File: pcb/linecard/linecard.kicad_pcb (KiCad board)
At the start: 6 copper layers, 716 parts, among them J1 CONN_ATX12V, J10 ARF6-08-S-D-A-K-TR, J11 SMPM, J12 SMPM, J13 XILINX_JTAG, J14 ARF6-08-S-D-A-K-TR, J2 LPJG47036AWNL, J3 CORTEX_DEBUG_ETM, J4 0532611071, J5 LPJG47036AWNL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

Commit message: Began layout of first few ports and left VSC8512
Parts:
- added R100: 1K, azonenberg_pcb:EIA_0402_RES_NOSILK, F.Cu at (65.0, 45.0)
- added R101: 10K, azonenberg_pcb:EIA_0402_RES_NOSILK, F.Cu at (65.0, 46.5)
- added TP23: TESTPOINT, azonenberg_pcb:TESTPOINT_SMT_0.5MM, F.Cu at (69.0, 45.0)
- added TP24: TESTPOINT, azonenberg_pcb:TESTPOINT_SMT_0.5MM, F.Cu at (69.0, 48.5)
- C100, C101, C102, C103, C104, C107, C108, C109, C110, C111, C112, C113, C116, C117, C118, C119, C120, C121, C124, C125, C126, C127, C128, C129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: moved to B.Cu
- R59, R92: value 10K -> 1K
- moved C146 152.5 mm to (-22.4, 91.7)
- moved C158 152.5 mm to (-19.3, 81.7)
- moved C162 152.5 mm to (-16.0, 72.7)
- moved C163 152.5 mm to (-16.0, 74.5)
- moved C169 152.5 mm to (-16.0, 76.3)
- moved C174 152.5 mm to (-16.0, 78.1)
- moved C61 152.5 mm to (-22.4, 83.9)
- moved C63 152.5 mm to (-22.4, 86.5)
- moved C76 152.5 mm to (-22.4, 89.1)
- moved C87 152.5 mm to (-19.3, 72.7)
- moved C94 152.5 mm to (-19.3, 76.3)
- moved C36 152.5 mm to (-22.6, 72.7)
- moved C39 152.5 mm to (-22.6, 74.5)
- moved C85 152.5 mm to (-22.6, 81.7)
- moved J10 152.4 mm to (36.4, 35.2)
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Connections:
- U10 pad R2: unconnected-(U10A-MDINT-PadR2) -> Net-(TP23-P1)
- U11 pad 4: /PHY 0 MDI/PHY0_M1_N -> /PHY 0 MDI/PHY0_M1_P
- U11 pad 5: /PHY 0 MDI/PHY0_M1_P -> /PHY 0 MDI/PHY0_M1_N
- U11 pad 6: /PHY 0 MDI/PHY0_D1_P -> /PHY 0 MDI/PHY0_D1_N
- U11 pad 7: /PHY 0 MDI/PHY0_D1_N -> /PHY 0 MDI/PHY0_D1_P
- U12 pad 1: /PHY 0 MDI/PHY0_M2_N -> /PHY 0 MDI/PHY0_M2_P
- U12 pad 10: /PHY 0 MDI/PHY0_D2_N -> /PHY 0 MDI/PHY0_D2_P
- U12 pad 2: /PHY 0 MDI/PHY0_M2_P -> /PHY 0 MDI/PHY0_M2_N
- U12 pad 9: /PHY 0 MDI/PHY0_D2_P -> /PHY 0 MDI/PHY0_D2_N
- U13 pad 1: /PHY 0 MDI/PHY1_M0_N -> /PHY 0 MDI/PHY1_M2_N
- U13 pad 10: /PHY 0 MDI/PHY1_D0_N -> /PHY 0 MDI/PHY1_D2_N
- U13 pad 2: /PHY 0 MDI/PHY1_M0_P -> /PHY 0 MDI/PHY1_M2_P
- U13 pad 4: /PHY 0 MDI/PHY1_M1_N -> /PHY 0 MDI/PHY1_M3_P
- U13 pad 5: /PHY 0 MDI/PHY1_M1_P -> /PHY 0 MDI/PHY1_M3_N
- U13 pad 6: /PHY 0 MDI/PHY1_D1_P -> /PHY 0 MDI/PHY1_D3_N
- U13 pad 7: /PHY 0 MDI/PHY1_D1_N -> /PHY 0 MDI/PHY1_D3_P
- U13 pad 9: /PHY 0 MDI/PHY1_D0_P -> /PHY 0 MDI/PHY1_D2_P
- U14 pad 1: /PHY 0 MDI/PHY1_M2_N -> /PHY 0 MDI/PHY1_M1_P
- U14 pad 10: /PHY 0 MDI/PHY1_D2_N -> /PHY 0 MDI/PHY1_D1_P
- U14 pad 2: /PHY 0 MDI/PHY1_M2_P -> /PHY 0 MDI/PHY1_M1_N
- U14 pad 4: /PHY 0 MDI/PHY1_M3_N -> /PHY 0 MDI/PHY1_M0_N
- U14 pad 5: /PHY 0 MDI/PHY1_M3_P -> /PHY 0 MDI/PHY1_M0_P
- U14 pad 6: /PHY 0 MDI/PHY1_D3_P -> /PHY 0 MDI/PHY1_D0_P
- U14 pad 7: /PHY 0 MDI/PHY1_D3_N -> /PHY 0 MDI/PHY1_D0_N
- U14 pad 9: /PHY 0 MDI/PHY1_D2_P -> /PHY 0 MDI/PHY1_D1_N
- U15 pad 1: /PHY 0 MDI/PHY2_M0_N -> /PHY 0 MDI/PHY2_M3_P
- U15 pad 10: /PHY 0 MDI/PHY2_D0_N -> /PHY 0 MDI/PHY2_D3_P
- U15 pad 2: /PHY 0 MDI/PHY2_M0_P -> /PHY 0 MDI/PHY2_M3_N
- U15 pad 4: /PHY 0 MDI/PHY2_M1_N -> /PHY 0 MDI/PHY2_M0_N
- U15 pad 5: /PHY 0 MDI/PHY2_M1_P -> /PHY 0 MDI/PHY2_M0_P
- U15 pad 6: /PHY 0 MDI/PHY2_D1_P -> /PHY 0 MDI/PHY2_D0_P
- U15 pad 7: /PHY 0 MDI/PHY2_D1_N -> /PHY 0 MDI/PHY2_D0_N
- U15 pad 9: /PHY 0 MDI/PHY2_D0_P -> /PHY 0 MDI/PHY2_D3_N
- U16 pad 1: /PHY 0 MDI/PHY2_M2_N -> /PHY 0 MDI/PHY2_M1_N
- U16 pad 10: /PHY 0 MDI/PHY2_D2_N -> /PHY 0 MDI/PHY2_D1_N
- U16 pad 2: /PHY 0 MDI/PHY2_M2_P -> /PHY 0 MDI/PHY2_M1_P
- U16 pad 4: /PHY 0 MDI/PHY2_M3_N -> /PHY 0 MDI/PHY2_M2_P
- U16 pad 5: /PHY 0 MDI/PHY2_M3_P -> /PHY 0 MDI/PHY2_M2_N
- U16 pad 6: /PHY 0 MDI/PHY2_D3_P -> /PHY 0 MDI/PHY2_D2_N
- U16 pad 7: /PHY 0 MDI/PHY2_D3_N -> /PHY 0 MDI/PHY2_D2_P
- U16 pad 9: /PHY 0 MDI/PHY2_D2_P -> /PHY 0 MDI/PHY2_D1_P
- U17 pad 1: /PHY 0 MDI/PHY3_M0_N -> /PHY 0 MDI/PHY3_M1_N
- U17 pad 10: /PHY 0 MDI/PHY3_D0_N -> /PHY 0 MDI/PHY3_D1_N
- U17 pad 2: /PHY 0 MDI/PHY3_M0_P -> /PHY 0 MDI/PHY3_M1_P
- U17 pad 4: /PHY 0 MDI/PHY3_M1_N -> /PHY 0 MDI/PHY3_M2_P
- U17 pad 5: /PHY 0 MDI/PHY3_M1_P -> /PHY 0 MDI/PHY3_M2_N
- U17 pad 6: /PHY 0 MDI/PHY3_D1_P -> /PHY 0 MDI/PHY3_D2_N
- U17 pad 7: /PHY 0 MDI/PHY3_D1_N -> /PHY 0 MDI/PHY3_D2_P
- U17 pad 9: /PHY 0 MDI/PHY3_D0_P -> /PHY 0 MDI/PHY3_D1_P
- U18 pad 1: /PHY 0 MDI/PHY3_M2_N -> /PHY 0 MDI/PHY3_M3_P
- U18 pad 10: /PHY 0 MDI/PHY3_D2_N -> /PHY 0 MDI/PHY3_D3_P
- U18 pad 2: /PHY 0 MDI/PHY3_M2_P -> /PHY 0 MDI/PHY3_M3_N
- U18 pad 4: /PHY 0 MDI/PHY3_M3_N -> /PHY 0 MDI/PHY3_M0_N
- U18 pad 5: /PHY 0 MDI/PHY3_M3_P -> /PHY 0 MDI/PHY3_M0_P
- U18 pad 6: /PHY 0 MDI/PHY3_D3_P -> /PHY 0 MDI/PHY3_D0_P
- U18 pad 7: /PHY 0 MDI/PHY3_D3_N -> /PHY 0 MDI/PHY3_D0_N
- U18 pad 9: /PHY 0 MDI/PHY3_D2_P -> /PHY 0 MDI/PHY3_D3_N
- U35 pad R2: unconnected-(U35A-MDINT-PadR2) -> Net-(TP24-P1)
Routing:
- net /GND: track 0.00 -> 509.9 mm, vias 0 -> 216
- net /1V0: track 0.00 -> 84.0 mm, vias 0 -> 80
- net /3V3: track 0.00 -> 82.2 mm
- net /PHY 0 MDI/PHY0_D3_N: track 0.00 -> 51.5 mm, vias 0 -> 1
- net /PHY 0 MDI/PHY0_D3_P: track 0.00 -> 51.4 mm, vias 0 -> 1
- net /PHY 0 MDI/PHY0_D2_N: track 0.00 -> 49.7 mm, vias 0 -> 1
- net /PHY 0 MDI/PHY0_D2_P: track 0.00 -> 49.7 mm, vias 0 -> 1
- net /PHY 0 MDI/PHY0_D1_N: track 0.00 -> 47.8 mm, vias 0 -> 1
- net /PHY 0 MDI/PHY0_D1_P: track 0.00 -> 47.7 mm, vias 0 -> 1
- net /PHY 0 MDI/PHY0_D0_N: track 0.00 -> 45.8 mm, vias 0 -> 1
- net /PHY 0 MDI/PHY0_D0_P: track 0.00 -> 45.7 mm, vias 0 -> 1
- net /PHY 0 MDI/PHY1_D3_N: track 0.00 -> 44.2 mm, vias 0 -> 1
- net /PHY 0 MDI/PHY1_D3_P: track 0.00 -> 44.1 mm, vias 0 -> 1
- net /PHY 0 Power/A2V5_VSC: track 0.00 -> 41.2 mm, vias 0 -> 28
- net /PHY 0 Power/A1V0_VSC: track 0.00 -> 33.3 mm, vias 0 -> 24
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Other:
- board outline added: 185 x 103.5 mm

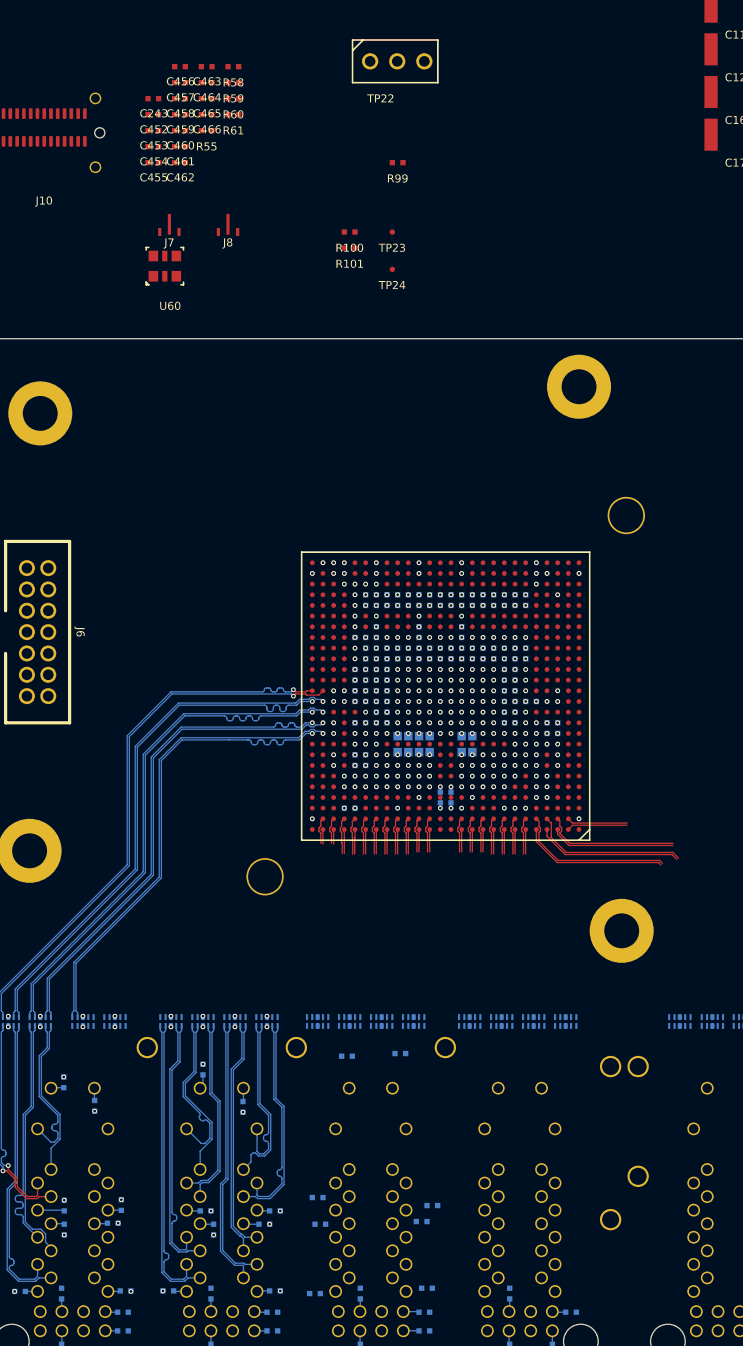
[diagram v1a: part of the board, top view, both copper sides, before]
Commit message: Update waiting for new part from vendor
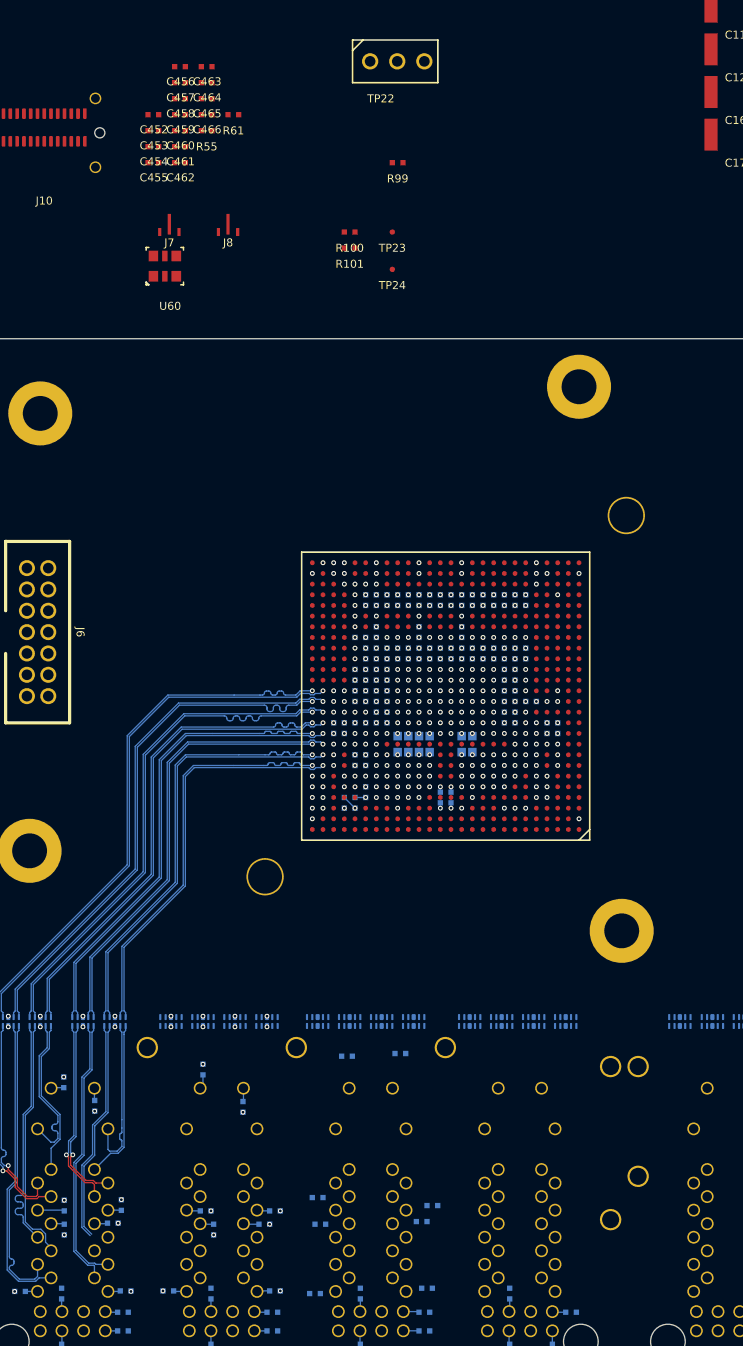
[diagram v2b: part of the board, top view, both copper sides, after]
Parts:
- C243, R58, R59, R60: moved to B.Cu
- moved R59 67.9 mm to (65.0, 98.0)
- moved R60 66.2 mm to (66.5, 97.5), turned to -90 degrees
- moved R58 63.3 mm to (64.0, 92.0)
- moved C243 61.0 mm to (64.0, 91.0), turned to 180 degrees
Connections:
- U13 pad 1: /PHY 0 MDI/PHY1_M2_N -> /PHY 0 MDI/PHY1_M2_P
- U13 pad 10: /PHY 0 MDI/PHY1_D2_N -> /PHY 0 MDI/PHY1_D2_P
- U13 pad 2: /PHY 0 MDI/PHY1_M2_P -> /PHY 0 MDI/PHY1_M2_N
- U13 pad 4: /PHY 0 MDI/PHY1_M3_P -> /PHY 0 MDI/PHY1_M3_N
- U13 pad 5: /PHY 0 MDI/PHY1_M3_N -> /PHY 0 MDI/PHY1_M3_P
- U13 pad 6: /PHY 0 MDI/PHY1_D3_N -> /PHY 0 MDI/PHY1_D3_P
- U13 pad 7: /PHY 0 MDI/PHY1_D3_P -> /PHY 0 MDI/PHY1_D3_N
- U13 pad 9: /PHY 0 MDI/PHY1_D2_P -> /PHY 0 MDI/PHY1_D2_N
- U14 pad 1: /PHY 0 MDI/PHY1_M1_P -> /PHY 0 MDI/PHY1_M0_N
- U14 pad 10: /PHY 0 MDI/PHY1_D1_P -> /PHY 0 MDI/PHY1_D0_N
- U14 pad 2: /PHY 0 MDI/PHY1_M1_N -> /PHY 0 MDI/PHY1_M0_P
- U14 pad 4: /PHY 0 MDI/PHY1_M0_N -> /PHY 0 MDI/PHY1_M1_N
- U14 pad 5: /PHY 0 MDI/PHY1_M0_P -> /PHY 0 MDI/PHY1_M1_P
- U14 pad 6: /PHY 0 MDI/PHY1_D0_P -> /PHY 0 MDI/PHY1_D1_P
- U14 pad 7: /PHY 0 MDI/PHY1_D0_N -> /PHY 0 MDI/PHY1_D1_N
- U14 pad 9: /PHY 0 MDI/PHY1_D1_N -> /PHY 0 MDI/PHY1_D0_P
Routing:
- net /PHY 0 MDI/PHY1_D2_N: track 0.00 -> 42.6 mm, vias 0 -> 1
- net /PHY 0 MDI/PHY1_D2_P: track 0.00 -> 41.0 mm, vias 0 -> 1
- net /PHY 0 MDI/PHY1_D1_N: track 0.00 -> 40.5 mm, vias 0 -> 1
- net /PHY 0 MDI/PHY1_D1_P: track 0.00 -> 40.5 mm, vias 0 -> 1
- net /PHY 0 MDI/PHY1_D0_N: track 0.00 -> 38.5 mm, vias 0 -> 1
- net /PHY 0 MDI/PHY1_D0_P: track 0.00 -> 38.4 mm, vias 0 -> 1
- net /PHY 0 MDI/PHY2_M2_N: track 27.2 -> 0.00 mm
- net /PHY 0 MDI/PHY2_M2_P: track 27.2 -> 0.00 mm
- net /PHY 0 MDI/PHY1_M2_N: track 0.00 -> 25.4 mm
- net /PHY 0 MDI/PHY1_M2_P: track 0.00 -> 25.3 mm
- net /PHY 0 MDI/PHY3_M2_N: track 25.2 -> 0.00 mm
- net /PHY 0 MDI/PHY3_M2_P: track 25.1 -> 0.00 mm
- net /PHY 0 MDI/PHY2_M1_P: track 24.0 -> 0.00 mm
- net /PHY 0 MDI/PHY2_M1_N: track 23.9 -> 0.00 mm
- net /PHY 0 MDI/PHY3_M1_P: track 22.1 -> 0.00 mm
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
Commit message: COntinued routing baseT pairs on left PHY
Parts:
- removed C193, C194, C195, C196, C197, C198, C199, C200, C201, C202, C203, C204, C205, C206, C207, C208, C209, C210, C211, C212, C213, C214, C215, C216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: 0.1 uF, azonenberg_pcb:EIA_0402_CAP_NOSILK
- C105, C106, C114, C115, C122, C123, C138, C139, C141, C142, C144, C145, C147, C149, C150, C154, C155, C156, C160, C161, C164, C165, C166, C167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: moved to B.Cu
- J2, J5, J9: value LPJG47036AWNL -> LPJT476156AENL; footprint azonenberg_pcb:CONN_LINKPP_LPJG47036AWNL -> azonenberg_pcb:CONN_LINKPP_LPJT476156AENL
- moved C146 124.3 mm to (100.8, 75.2)
- moved C61 124.3 mm to (100.8, 67.4)
- moved C63 124.3 mm to (100.8, 70.0)
- moved C76 124.3 mm to (100.8, 72.6)
- moved C48 110.2 mm to (99.0, 84.0)
- moved C49 110.2 mm to (99.0, 85.5)
- moved C39 106.8 mm to (81.5, 98.2), turned to -90 degrees
- moved C36 106.2 mm to (80.5, 98.2), turned to -90 degrees
- moved C54 100.9 mm to (92.2, 81.2)
- moved C55 100.9 mm to (92.2, 82.8)
- moved C47 97.2 mm to (85.5, 77.0)
- moved C130 97.0 mm to (98.5, 79.2)
- moved C131 97.0 mm to (98.5, 80.8)
- moved C148 97.0 mm to (101.0, 80.8)
- moved C87 95.8 mm to (74.0, 94.8), turned to 90 degrees
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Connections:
- J2 pad A1: Net-(J2A-MD2_CT) -> /PHY 0 MDI/PHY0_M0_P
- J2 pad A10: /PHY 0 MDI/PHY0_M0_N -> /GND
- J2 pad A11: /PHY 0 MDI/PHY0_M0_P -> /3V3
- J2 pad A12: Net-(J2A-MD0_CT) -> /PHY 0 MDI/PHY0_LED1_N
- J2 pad A13: /PHY 0 MDI/PHY0_LED1_N -> /3V3
- J2 pad A14: /3V3 -> /PHY 0 MDI/PHY0_LED0_N
- J2 pad A2: /PHY 0 MDI/PHY0_M2_N -> /PHY 0 MDI/PHY0_M0_N
- J2 pad A3: /PHY 0 MDI/PHY0_M2_P -> /PHY 0 MDI/PHY0_M1_P
- J2 pad A4: /PHY 0 MDI/PHY0_M1_P -> /PHY 0 MDI/PHY0_M1_N
- J2 pad A5: /PHY 0 MDI/PHY0_M1_N -> /PHY 0 MDI/PHY0_M2_P
- J2 pad A6: Net-(J2A-MD1_CT) -> /PHY 0 MDI/PHY0_M2_N
- J2 pad A7: Net-(J2A-MD3_CT) -> /PHY 0 MDI/PHY0_M3_P
- J2 pad A8: /PHY 0 MDI/PHY0_M3_P -> /PHY 0 MDI/PHY0_M3_N
- J2 pad A9: /PHY 0 MDI/PHY0_M3_N -> unconnected-(J2A-NC-PadA9)
- J2 pad B1: Net-(J2B-MD2_CT) -> /PHY 0 MDI/PHY1_M0_P
- J2 pad B10: /PHY 0 MDI/PHY1_M0_N -> /GND
- J2 pad B11: /PHY 0 MDI/PHY1_M0_P -> /3V3
- J2 pad B12: Net-(J2B-MD0_CT) -> /PHY 0 MDI/PHY1_LED1_N
- J2 pad B13: /PHY 0 MDI/PHY1_LED1_N -> /3V3
- J2 pad B14: /3V3 -> /PHY 0 MDI/PHY1_LED0_N
- J2 pad B2: /PHY 0 MDI/PHY1_M2_N -> /PHY 0 MDI/PHY1_M0_N
- J2 pad B3: /PHY 0 MDI/PHY1_M2_P -> /PHY 0 MDI/PHY1_M1_P
- J2 pad B4: /PHY 0 MDI/PHY1_M1_P -> /PHY 0 MDI/PHY1_M1_N
- J2 pad B5: /PHY 0 MDI/PHY1_M1_N -> /PHY 0 MDI/PHY1_M2_P
- J2 pad B6: Net-(J2B-MD1_CT) -> /PHY 0 MDI/PHY1_M2_N
- J2 pad B7: Net-(J2B-MD3_CT) -> /PHY 0 MDI/PHY1_M3_P
- J2 pad B8: /PHY 0 MDI/PHY1_M3_P -> /PHY 0 MDI/PHY1_M3_N
- J2 pad B9: /PHY 0 MDI/PHY1_M3_N -> unconnected-(J2B-NC-PadB9)
- J2 pad C1: Net-(J2C-MD2_CT) -> /PHY 0 MDI/PHY2_M0_P
- J2 pad C10: /PHY 0 MDI/PHY2_M0_N -> /GND
- J2 pad C11: /PHY 0 MDI/PHY2_M0_P -> /3V3
- J2 pad C12: Net-(J2C-MD0_CT) -> /PHY 0 MDI/PHY2_LED1_N
- J2 pad C13: /PHY 0 MDI/PHY2_LED1_N -> /3V3
- J2 pad C14: /3V3 -> /PHY 0 MDI/PHY2_LED0_N
- J2 pad C2: /PHY 0 MDI/PHY2_M2_N -> /PHY 0 MDI/PHY2_M0_N
- J2 pad C3: /PHY 0 MDI/PHY2_M2_P -> /PHY 0 MDI/PHY2_M1_P
- J2 pad C4: /PHY 0 MDI/PHY2_M1_P -> /PHY 0 MDI/PHY2_M1_N
- J2 pad C5: /PHY 0 MDI/PHY2_M1_N -> /PHY 0 MDI/PHY2_M2_P
- J2 pad C6: Net-(J2C-MD1_CT) -> /PHY 0 MDI/PHY2_M2_N
- J2 pad C7: Net-(J2C-MD3_CT) -> /PHY 0 MDI/PHY2_M3_P
- J2 pad C8: /PHY 0 MDI/PHY2_M3_P -> /PHY 0 MDI/PHY2_M3_N
- J2 pad C9: /PHY 0 MDI/PHY2_M3_N -> unconnected-(J2C-NC-PadC9)
- J2 pad D1: Net-(J2D-MD2_CT) -> /PHY 0 MDI/PHY3_M0_P
- J2 pad D10: /PHY 0 MDI/PHY3_M0_N -> /GND
- J2 pad D11: /PHY 0 MDI/PHY3_M0_P -> /3V3
- J2 pad D12: Net-(J2D-MD0_CT) -> /PHY 0 MDI/PHY3_LED1_N
- J2 pad D13: /PHY 0 MDI/PHY3_LED1_N -> /3V3
- J2 pad D14: /3V3 -> /PHY 0 MDI/PHY3_LED0_N
- J2 pad D2: /PHY 0 MDI/PHY3_M2_N -> /PHY 0 MDI/PHY3_M0_N
- J2 pad D3: /PHY 0 MDI/PHY3_M2_P -> /PHY 0 MDI/PHY3_M1_P
- J2 pad D4: /PHY 0 MDI/PHY3_M1_P -> /PHY 0 MDI/PHY3_M1_N
- J2 pad D5: /PHY 0 MDI/PHY3_M1_N -> /PHY 0 MDI/PHY3_M2_P
- J2 pad D6: Net-(J2D-MD1_CT) -> /PHY 0 MDI/PHY3_M2_N
- J2 pad D7: Net-(J2D-MD3_CT) -> /PHY 0 MDI/PHY3_M3_P
- J2 pad D8: /PHY 0 MDI/PHY3_M3_P -> /PHY 0 MDI/PHY3_M3_N
- J2 pad D9: /PHY 0 MDI/PHY3_M3_N -> unconnected-(J2D-NC-PadD9)
- J2 pad E1: Net-(J2E-MD2_CT) -> /PHY 0 MDI/PHY4_M0_P
- J2 pad E10: /PHY 0 MDI/PHY4_M0_N -> /GND
- J2 pad E11: /PHY 0 MDI/PHY4_M0_P -> /3V3
- J2 pad E12: Net-(J2E-MD0_CT) -> /PHY 0 MDI/PHY4_LED1_N
- J2 pad E13: /PHY 0 MDI/PHY4_LED1_N -> /3V3
- J2 pad E14: /3V3 -> /PHY 0 MDI/PHY4_LED0_N
- J2 pad E2: /PHY 0 MDI/PHY4_M2_N -> /PHY 0 MDI/PHY4_M0_N
- J2 pad E3: /PHY 0 MDI/PHY4_M2_P -> /PHY 0 MDI/PHY4_M1_P
- J2 pad E4: /PHY 0 MDI/PHY4_M1_P -> /PHY 0 MDI/PHY4_M1_N
- J2 pad E5: /PHY 0 MDI/PHY4_M1_N -> /PHY 0 MDI/PHY4_M2_P
- J2 pad E6: Net-(J2E-MD1_CT) -> /PHY 0 MDI/PHY4_M2_N
- J2 pad E7: Net-(J2E-MD3_CT) -> /PHY 0 MDI/PHY4_M3_P
- J2 pad E8: /PHY 0 MDI/PHY4_M3_P -> /PHY 0 MDI/PHY4_M3_N
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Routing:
- net /GND: track 512.8 -> 906.0 mm, vias 216 -> 285
- net /3V3: track 82.2 -> 287.3 mm
- net /2V5: track 5.30 -> 59.7 mm, vias 4 -> 21
- net /PHY 0 MDI/PHY11_D3_N: track 0.00 -> 42.5 mm, vias 0 -> 1
- net /PHY 0 MDI/PHY11_D3_P: track 0.00 -> 42.3 mm, vias 0 -> 1
- net /PHY 0 MDI/PHY10_D0_N: track 0.00 -> 40.4 mm, vias 0 -> 1
- net /PHY 0 MDI/PHY10_D0_P: track 0.00 -> 40.4 mm, vias 0 -> 1
- net /PHY 0 MDI/PHY10_D1_N: track 0.00 -> 38.8 mm, vias 0 -> 1
- net /PHY 0 MDI/PHY10_D1_P: track 0.00 -> 37.9 mm, vias 0 -> 1
- net /PHY 0 MDI/PHY10_D2_N: track 0.00 -> 37.6 mm, vias 0 -> 1
- net /PHY 0 MDI/PHY10_D2_P: track 0.00 -> 37.5 mm, vias 0 -> 1
- net /PHY 0 MDI/PHY10_D3_N: track 0.00 -> 36.0 mm, vias 0 -> 1
- net /PHY 0 MDI/PHY10_D3_P: track 0.00 -> 35.9 mm, vias 0 -> 1
- net /PHY 0 Power/A1V0_VSC_SERDES2: track 0.00 -> 35.5 mm, vias 2 -> 16
- net /PHY 0 MDI/PHY2_D3_N: track 0.00 -> 35.0 mm
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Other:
- board size 185 x 103.5 mm -> 185 x 93.5 mm
- board text added: "LATENTRED 24-Port QSGMII Non-PoE Line Card A. Zonenberg / v0.1 / 2024-12-13"

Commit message: Left half getting close to finished
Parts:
- R55: moved to B.Cu
- moved TP1 187.3 mm to (53.5, 86.0)
- moved C452 68.2 mm to (95.5, 81.5)
- moved C143 62.7 mm to (107.0, 75.2)
- moved C153 62.7 mm to (112.0, 81.1)
- moved C159 62.7 mm to (112.0, 85.0)
- moved C33 62.7 mm to (112.0, 73.3)
- moved C56 62.7 mm to (112.0, 77.2)
- moved C78 62.7 mm to (107.0, 72.6)
- moved L1 62.7 mm to (107.0, 77.8)
- moved L2 62.7 mm to (107.0, 80.4)
- moved L3 62.7 mm to (107.0, 83.0)
- moved L4 62.7 mm to (107.0, 85.6)
- moved C453 62.6 mm to (92.5, 78.0), turned to 180 degrees
- moved C454 62.2 mm to (92.5, 79.0), turned to 180 degrees
- moved U60 57.3 mm to (96.0, 79.0), turned to 90 degrees
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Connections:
- C453 pad 2: /PHY 0 Backend/REFCLK_AC_P -> /PHY 0 Backend/REFCLK_AC_N
- C454 pad 2: /PHY 0 Backend/REFCLK_AC_N -> /PHY 0 Backend/REFCLK_AC_P
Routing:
- net Net-(U10B-PHY1_LED0): track 23.7 -> 93.6 mm
- net Net-(U10B-PHY0_LED0): track 29.7 -> 96.1 mm
- net Net-(U10B-PHY0_LED1): track 23.4 -> 89.3 mm
- net Net-(U10B-PHY1_LED1): track 28.6 -> 92.1 mm
- net Net-(U10B-PHY5_LED1): track 4.28 -> 67.2 mm, vias 0 -> 1
- net /PHY 0 Backend/JTAG_TCK: track 0.00 -> 58.5 mm, vias 1 -> 0
- net Net-(U10B-PHY4_LED1): track 4.93 -> 63.3 mm, vias 0 -> 1
- net Net-(U10B-PHY3_LED0): track 25.1 -> 82.5 mm
- net Net-(U10B-PHY2_LED0): track 24.7 -> 81.5 mm
- net Net-(U10B-PHY7_LED1): track 5.80 -> 60.4 mm, vias 1 -> 2
- net Net-(U10B-PHY6_LED0): track 2.70 -> 56.3 mm, vias 0 -> 1
- net Net-(U10B-PHY2_LED1): track 21.4 -> 74.3 mm
- net Net-(U10B-PHY3_LED1): track 30.4 -> 83.1 mm
- net Net-(U10B-PHY7_LED0): track 5.50 -> 57.0 mm, vias 1 -> 2
- net /PHY 0 Backend/JTAG_TMS: track 0.00 -> 50.1 mm, vias 1 -> 0
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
